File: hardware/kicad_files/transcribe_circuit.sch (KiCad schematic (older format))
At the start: 23 parts, among them J1 europower, J2 RS232_SERIAL, J3 RS232_DSUB, J4 MIDI_IN_TRS, J5 MIDI_IN_DIN, J6 MIDI_OUT_TRS, J7 MIDI_OUT_DIN, U1 ProMicro, U2 MAX232, U3 6N137, U4 4069, U5 usbHostMini, U6 L78L33_TO92

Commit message: small pcb fixes
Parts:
- added D2: 1N4148, Diode_THT:D_T-1_P5.08mm_Horizontal, symbol Device:D
- C1: footprint Capacitor_THT:CP_Radial_D6.3mm_P2.50mm -> Capacitor_THT:CP_Radial_D5.0mm_P2.50mm
- C2, C3, C4, C5: footprint Capacitor_THT:C_Disc_D3.0mm_W1.6mm_P2.50mm -> Capacitor_THT:C_Disc_D4.3mm_W1.9mm_P5.00mm
- D1: footprint Diode_THT:D_A-405_P7.62mm_Horizontal -> Diode_THT:D_T-1_P5.08mm_Horizontal
- J1: footprint Connector_PinHeader_2.54mm:PinHeader_2x08_P2.54mm_Vertical -> lib_fp:PinHeader_2x08_P2.54_Euro
- J2, J4, J6: footprint Connector_Audio:Tayda_3.5mm_stereo_TRS_jack_A-853 -> lib_fp:Tayda_3.5mm_stereo_TRS_jack_A-853
- J5, J7: footprint Connector_DIN:Tayda5pinMidi-A1010 -> lib_fp:Tayda5pinMidi-A1010
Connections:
- net +5V: now also D2.1 (K); no longer J1.11 (Pin_11), J1.12 (Pin_12)
- new net: D2.2 (A), J1.11 (Pin_11), J1.12 (Pin_12)
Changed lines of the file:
@@
 F 0 "D1" V 8529 2129 50  0000 L CNN
 F 1 "1N4148" H 8475 1950 50  0000 L CNN
-F 2 "Diode_THT:D_A-405_P7.62mm_Horizontal" H 8575 2050 50  0001 C CNN
+F 2 "Diode_THT:D_T-1_P5.08mm_Horizontal" H 8575 2050 50  0001 C CNN
 F 3 "~" H 8575 2050 50  0001 C CNN
 	1    8575 2050
@@
 F 0 "J4" H 7632 3700 50  0000 C CNN
 F 1 "MIDI_IN_TRS" H 7632 3609 50  0000 C CNN
-F 2 "Connector_Audio:Tayda_3.5mm_stereo_TRS_jack_A-853" H 7650 3375 50  0001 C CNN
+F 2 "lib_fp:Tayda_3.5mm_stereo_TRS_jack_A-853" H 7650 3375 50  0001 C CNN
 F 3 "~" H 7650 3375 50  0001 C CNN
 	1    7650 3375
@@
 F 0 "J6" H 7707 6025 50  0000 C CNN
 F 1 "MIDI_OUT_TRS" H 7707 5934 50  0000 C CNN
-F 2 "Connector_Audio:Tayda_3.5mm_stereo_TRS_jack_A-853" H 7725 5700 50  0001 C CNN
+F 2 "lib_fp:Tayda_3.5mm_stereo_TRS_jack_A-853" H 7725 5700 50  0001 C CNN
 F 3 "~" H 7725 5700 50  0001 C CNN
 	1    7725 5700
@@
 F 0 "C2" H 4265 2971 50  0000 L CNN
 F 1 "0.1u" H 4265 2880 50  0000 L CNN
-F 2 "Capacitor_THT:C_Disc_D3.0mm_W1.6mm_P2.50mm" H 4188 2775 50  0001 C CNN
+F 2 "Capacitor_THT:C_Disc_D4.3mm_W1.9mm_P5.00mm" H 4188 2775 50  0001 C CNN
 F 3 "~" H 4150 2925 50  0001 C CNN
 	1    4150 2925
@@
 F 0 "C4" H 6365 2971 50  0000 L CNN
 F 1 "0.1u" H 6365 2880 50  0000 L CNN
-F 2 "Capacitor_THT:C_Disc_D3.0mm_W1.6mm_P2.50mm" H 6288 2775 50  0001 C CNN
+F 2 "Capacitor_THT:C_Disc_D4.3mm_W1.9mm_P5.00mm" H 6288 2775 50  0001 C CNN
 F 3 "~" H 6250 2925 50  0001 C CNN
 	1    6250 2925
@@
 F 0 "C3" V 6000 3275 50  0000 C CNN
 F 1 "0.1u" V 6300 3275 50  0000 C CNN
-F 2 "Capacitor_THT:C_Disc_D3.0mm_W1.6mm_P2.50mm" H 6188 3125 50  0001 C CNN
+F 2 "Capacitor_THT:C_Disc_D4.3mm_W1.9mm_P5.00mm" H 6188 3125 50  0001 C CNN
 F 3 "~" H 6150 3275 50  0001 C CNN
 	1    6150 3275
@@
 F 0 "C5" V 6150 3575 50  0000 C CNN
 F 1 "0.1u" V 6450 3575 50  0000 C CNN
-F 2 "Capacitor_THT:C_Disc_D3.0mm_W1.6mm_P2.50mm" H 6338 3425 50  0001 C CNN
+F 2 "Capacitor_THT:C_Disc_D4.3mm_W1.9mm_P5.00mm" H 6338 3425 50  0001 C CNN
 F 3 "~" H 6300 3575 50  0001 C CNN
 	1    6300 3575
@@
 F 0 "J2" H 4132 1900 50  0000 C CNN
 F 1 "RS232_SERIAL" H 4025 1800 50  0000 C CNN
-F 2 "Connector_Audio:Tayda_3.5mm_stereo_TRS_jack_A-853" H 4150 1575 50  0001 C CNN
+F 2 "lib_fp:Tayda_3.5mm_stereo_TRS_jack_A-853" H 4150 1575 50  0001 C CNN
 F 3 "~" H 4150 1575 50  0001 C CNN
 	1    4150 1575
@@
 F 0 "J7" H 9950 5525 50  0000 C CNN
 F 1 "MIDI_OUT_DIN" H 9950 5434 50  0000 C CNN
-F 2 "Connector_DIN:Tayda5pinMidi-A1010" H 9950 5800 50  0001 C CNN
+F 2 "lib_fp:Tayda5pinMidi-A1010" H 9950 5800 50  0001 C CNN
 F 3 "http://www.mouser.com/ds/2/18/40_c091_abd_e-75918.pdf" H 9950 5800 50  0001 C CNN
 	1    9950 5800
@@
 F 0 "J5" H 9850 3025 50  0000 C CNN
 F 1 "MIDI_IN_DIN" H 9850 2934 50  0000 C CNN
-F 2 "Connector_DIN:Tayda5pinMidi-A1010" H 9850 3300 50  0001 C CNN
+F 2 "lib_fp:Tayda5pinMidi-A1010" H 9850 3300 50  0001 C CNN
 F 3 "http://www.mouser.com/ds/2/18/40_c091_abd_e-75918.pdf" H 9850 3300 50  0001 C CNN
 	1    9850 3300
@@
 F 0 "C1" H 3618 1721 50  0000 L CNN
 F 1 "100uf" H 3618 1630 50  0000 L CNN
-F 2 "Capacitor_THT:CP_Radial_D6.3mm_P2.50mm" H 3538 1525 50  0001 C CNN
+F 2 "Capacitor_THT:CP_Radial_D5.0mm_P2.50mm" H 3538 1525 50  0001 C CNN
 F 3 "~" H 3500 1675 50  0001 C CNN
 	1    3500 1675
@@
 F 0 "J1" H 1300 3050 50  0000 C CNN
 F 1 "europower" H 1300 3141 50  0000 C CNN
-F 2 "Connector_PinHeader_2.54mm:PinHeader_2x08_P2.54mm_Vertical" H 1250 3675 50  0001 C CNN
+F 2 "lib_fp:PinHeader_2x08_P2.54_Euro" H 1250 3675 50  0001 C CNN
 F 3 "~" H 1250 3675 50  0001 C CNN
 	1    1250 3675
@@
 L power:+5V #PWR06
 U 1 1 5E281F93
-P 1725 3375
-F 0 "#PWR06" H 1725 3225 50  0001 C CNN
-F 1 "+5V" H 1740 3548 50  0000 C CNN
-F 2 "" H 1725 3375 50  0001 C CNN
-F 3 "" H 1725 3375 50  0001 C CNN
-	1    1725 3375
-	1    0    0    -1
-$EndComp
-$Comp
-L power:+5V #PWR01
-U 1 1 5E2863EC
-P 700 3375
-F 0 "#PWR01" H 700 3225 50  0001 C CNN
-F 1 "+5V" H 715 3548 50  0000 C CNN
-F 2 "" H 700 3375 50  0001 C CNN
-F 3 "" H 700 3375 50  0001 C CNN
-	1    700  3375
-	1    0    0    -1
-$EndComp
-Wire Wire Line
-	950  3475 700  3475
-Wire Wire Line
-	700  3475 700  3375
+P 1750 3375
+F 0 "#PWR06" H 1750 3225 50  0001 C CNN
+F 1 "+5V" H 1765 3548 50  0000 C CNN
+F 2 "" H 1750 3375 50  0001 C CNN
+F 3 "" H 1750 3375 50  0001 C CNN
+	1    1750 3375
+	1    0    0    -1
+$EndComp
 NoConn ~ 950  3275
 NoConn ~ 950  3375
@@
 NoConn ~ 1450 3575
 NoConn ~ 950  3575
-$Comp
-L power:GND #PWR02
-U 1 1 5E29F868
-P 700 4000
-F 0 "#PWR02" H 700 3750 50  0001 C CNN
-F 1 "GND" H 705 3827 50  0000 C CNN
-F 2 "" H 700 4000 50  0001 C CNN
-F 3 "" H 700 4000 50  0001 C CNN
-	1    700  4000
-	1    0    0    -1
-$EndComp
 $Comp
 L power:GND #PWR07
@@
 $EndComp
 Wire Wire Line
-	950  3675 700  3675
-Wire Wire Line
-	700  3675 700  3775
-Wire Wire Line
-	950  3875 700  3875
-Connection ~ 700  3875
-Wire Wire Line
-	700  3875 700  4000
-Wire Wire Line
-	950  3775 700  3775
-Connection ~ 700  3775
-Wire Wire Line
-	700  3775 700  3875
-Wire Wire Line
-	1725 3475 1725 3375
-Wire Wire Line
-	1450 3475 1725 3475
-Wire Wire Line
 	1450 3675 1725 3675
 Wire Wire Line
@@
 Wire Wire Line
 	6225 2050 6225 2125
+$Comp
+L Device:D D2
+U 1 1 5E8284AF
+P 1600 3475
+F 0 "D2" H 1600 3259 50  0000 C CNN
+F 1 "1N4148" H 1600 3350 50  0000 C CNN
+F 2 "Diode_THT:D_T-1_P5.08mm_Horizontal" H 1600 3475 50  0001 C CNN
+F 3 "~" H 1600 3475 50  0001 C CNN
+	1    1600 3475
+	-1   0    0    1
+$EndComp
+Wire Wire Line
+	1750 3375 1750 3475
+Wire Wire Line
+	950  3475 1450 3475
+Connection ~ 1450 3475
+Wire Wire Line
+	950  3675 1450 3675
+Connection ~ 1450 3675
+Wire Wire Line
+	950  3775 1450 3775
+Connection ~ 1450 3775
+Wire Wire Line
+	950  3875 1450 3875
+Connection ~ 1450 3875
 $EndSCHEMATC

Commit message: update circuit to v0.2
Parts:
- added J8: Conn_01x06, Connector_PinSocket_2.54mm:PinSocket_1x06_P2.54mm_Vertical, symbol Connector_Generic:Conn_01x06
- J3: footprint Connector_Dsub:DSUB-9_Female_Vertical_P2.77x2.84mm_MountingHoles -> lib_fp:DSUB-9_Male_Vertical_Tayda
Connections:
- net +5V: now also J8.6 (Pin_6)
- net GND: now also J8.5 (Pin_5)
- net MISO_HOST: now also J8.2 (Pin_2)
- net MOSI_HOST: now also J8.1 (Pin_1)
- net RST_HOST: now also J8.4 (Pin_4)
- net SKC_HOST: now also J8.3 (Pin_3)
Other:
- note added: "bootloader breakout"
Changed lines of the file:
@@
 Sheet 1 1
 Title "_transcribe_"
-Date "2020-01-13"
-Rev "0.1"
+Date "2020-06-13"
+Rev "0.2"
 Comp "cyberboy666 & user43368831"
 Comment1 ""
@@
 F 0 "J3" H 6705 1452 50  0000 L CNN
 F 1 "RS232_DSUB" H 6705 1361 50  0000 L CNN
-F 2 "Connector_Dsub:DSUB-9_Female_Vertical_P2.77x2.84mm_MountingHoles" H 6525 1450 50  0001 C CNN
+F 2 "lib_fp:DSUB-9_Male_Vertical_Tayda" H 6525 1450 50  0001 C CNN
 F 3 " ~" H 6525 1450 50  0001 C CNN
 	1    6525 1450
@@
 	950  3875 1450 3875
 Connection ~ 1450 3875
+$Comp
+L Connector_Generic:Conn_01x06 J8
+U 1 1 5EE5600D
+P 4625 5900
+F 0 "J8" H 4543 5375 50  0000 C CNN
+F 1 "Conn_01x06" H 4543 5466 50  0000 C CNN
+F 2 "Connector_PinSocket_2.54mm:PinSocket_1x06_P2.54mm_Vertical" H 4625 5900 50  0001 C CNN
+F 3 "~" H 4625 5900 50  0001 C CNN
+	1    4625 5900
+	-1   0    0    1
+$EndComp
+Text GLabel 4900 5900 2    50   Input ~ 0
+SKC_HOST
+Text GLabel 4900 6000 2    50   Input ~ 0
+MISO_HOST
+Text GLabel 4900 6100 2    50   Input ~ 0
+MOSI_HOST
+Text GLabel 4900 5800 2    50   Input ~ 0
+RST_HOST
+$Comp
+L power:GND #PWR02
+U 1 1 5EE5C0CB
+P 5475 5700
+F 0 "#PWR02" H 5475 5450 50  0001 C CNN
+F 1 "GND" H 5480 5527 50  0000 C CNN
+F 2 "" H 5475 5700 50  0001 C CNN
+F 3 "" H 5475 5700 50  0001 C CNN
+	1    5475 5700
+	1    0    0    -1
+$EndComp
+$Comp
+L power:+5V #PWR01
+U 1 1 5EE5E849
+P 5200 5600
+F 0 "#PWR01" H 5200 5450 50  0001 C CNN
+F 1 "+5V" H 5215 5773 50  0000 C CNN
+F 2 "" H 5200 5600 50  0001 C CNN
+F 3 "" H 5200 5600 50  0001 C CNN
+	1    5200 5600
+	1    0    0    -1
+$EndComp
+Wire Wire Line
+	4825 6100 4900 6100
+Wire Wire Line
+	4825 6000 4900 6000
+Wire Wire Line
+	4825 5900 4900 5900
+Wire Wire Line
+	4825 5800 4900 5800
+Wire Wire Line
+	5475 5700 4825 5700
+Wire Wire Line
+	4825 5600 5200 5600
+Text Notes 4550 5325 0    39   ~ 0
+bootloader breakout
 $EndSCHEMATC

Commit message: refactored the code and updated circuit
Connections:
- net GND: no longer J2.RN, J2.TN
- no-connect marks 52 -> 54
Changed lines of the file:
@@
 Wire Wire Line
 	4350 1475 4500 1475
-Wire Wire Line
-	4500 1475 4500 1675
-Wire Wire Line
-	4350 1675 4500 1675
-Connection ~ 4500 1675
-Wire Wire Line
-	4500 1675 4500 1875
-Wire Wire Line
-	4350 1875 4500 1875
-Connection ~ 4500 1875
-Wire Wire Line
-	4500 1875 4500 1950
 $Comp
 L 4xxx:4069 U4
@@
 Text Notes 4550 5325 0    39   ~ 0
 bootloader breakout
+Wire Wire Line
+	4500 1475 4500 1950
+NoConn ~ 4350 1675
+NoConn ~ 4350 1875
 $EndSCHEMATC

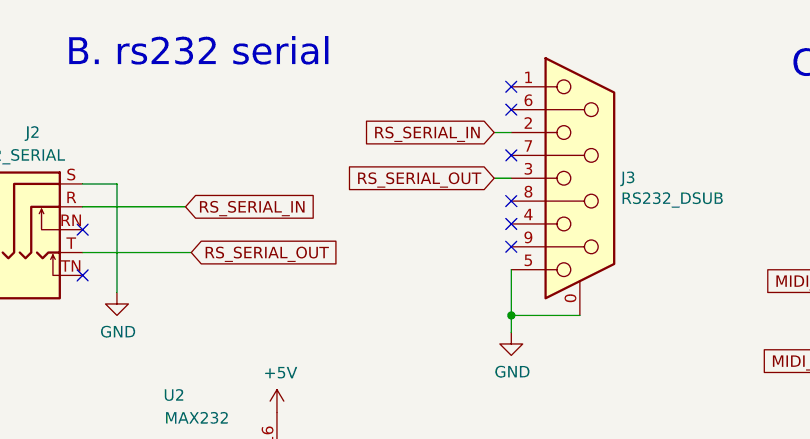
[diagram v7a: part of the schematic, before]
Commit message: update circuit to 0.3 and add note to build guide for <=0.2
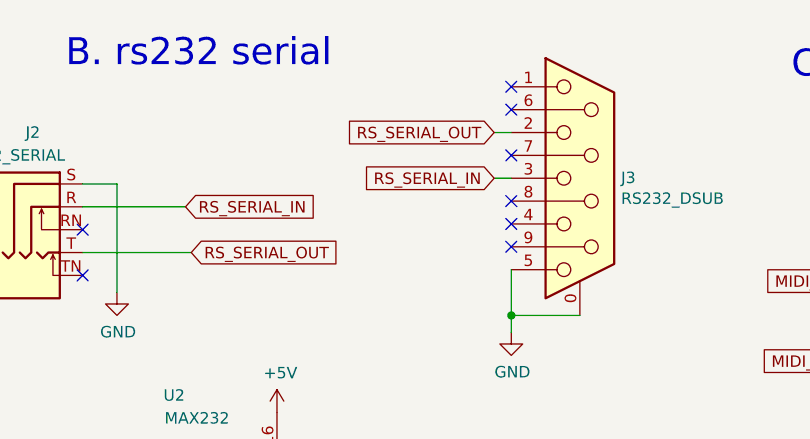
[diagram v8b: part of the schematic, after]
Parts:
- U6: footprint Package_TO_SOT_THT:TO-92_Inline -> Package_TO_SOT_THT:TO-92_HandSolder
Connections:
- net RS_SERIAL_IN: now also J3.3; no longer J3.2
- net RS_SERIAL_OUT: now also J3.2; no longer J3.3
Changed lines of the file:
@@
 Sheet 1 1
 Title "_transcribe_"
-Date "2020-06-13"
-Rev "0.2"
+Date "2020-09-23"
+Rev "0.3"
 Comp "cyberboy666 & user43368831"
 Comment1 ""
@@
 Text GLabel 4225 3775 0    50   Input ~ 0
 ALT_SERIAL_OUT
-Text GLabel 6150 1450 0    50   Input ~ 0
+Text GLabel 6150 1250 0    50   Input ~ 0
 RS_SERIAL_OUT
 Wire Wire Line
@@
 Text GLabel 4825 1775 2    50   Input ~ 0
 RS_SERIAL_OUT
-Text GLabel 6150 1250 0    50   Input ~ 0
+Text GLabel 6150 1450 0    50   Input ~ 0
 RS_SERIAL_IN
 Wire Wire Line
@@
 F 0 "U6" H 1300 5267 50  0000 C CNN
 F 1 "L78L33_TO92" H 1300 5176 50  0000 C CNN
-F 2 "Package_TO_SOT_THT:TO-92_Inline" H 1300 5250 50  0001 C CIN
+F 2 "Package_TO_SOT_THT:TO-92_HandSolder" H 1300 5250 50  0001 C CIN
 F 3 "http://www.st.com/content/ccc/resource/technical/document/datasheet/15/55/e5/aa/23/5b/43/fd/CD00000446.pdf/files/CD00000446.pdf/jcr:content/translations/en.CD00000446.pdf" H 1300 4975 50  0001 C CNN
 	1    1300 5025
